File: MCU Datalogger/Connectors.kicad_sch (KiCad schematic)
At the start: 4 parts, among them J1 Conn_01x04_Pin, J2 Conn_01x04_Pin, J3 Conn_01x09_Pin, J4 Conn_02x03_Odd_Even

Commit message: main: Assigned footprints to all parts
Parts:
- J1, J2: footprint (none) -> Connector_PinHeader_2.54mm:PinHeader_1x04_P2.54mm_Vertical
- J3: footprint (none) -> Connector_PinHeader_2.54mm:PinHeader_1x09_P2.54mm_Vertical
- J4: footprint (none) -> Connector_PinHeader_2.54mm:PinHeader_2x03_P2.54mm_Vertical
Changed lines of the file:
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@@
 			)
 		)
-		(property "Footprint" ""
+		(property "Footprint" "Connector_PinHeader_2.54mm:PinHeader_1x09_P2.54mm_Vertical"
 			(at 63.5 101.6 0)
 			(effects
@@
 			)
 		)
-		(property "Footprint" ""
+		(property "Footprint" "Connector_PinHeader_2.54mm:PinHeader_2x03_P2.54mm_Vertical"
 			(at 66.04 127 0)
 			(effects
@@
 			)
 		)
-		(property "Footprint" ""
+		(property "Footprint" "Connector_PinHeader_2.54mm:PinHeader_1x04_P2.54mm_Vertical"
 			(at 60.96 46.99 0)
 			(effects
@@
 			)
 		)
-		(property "Footprint" ""
+		(property "Footprint" "Connector_PinHeader_2.54mm:PinHeader_1x04_P2.54mm_Vertical"
 			(at 63.5 69.85 0)
 			(effects

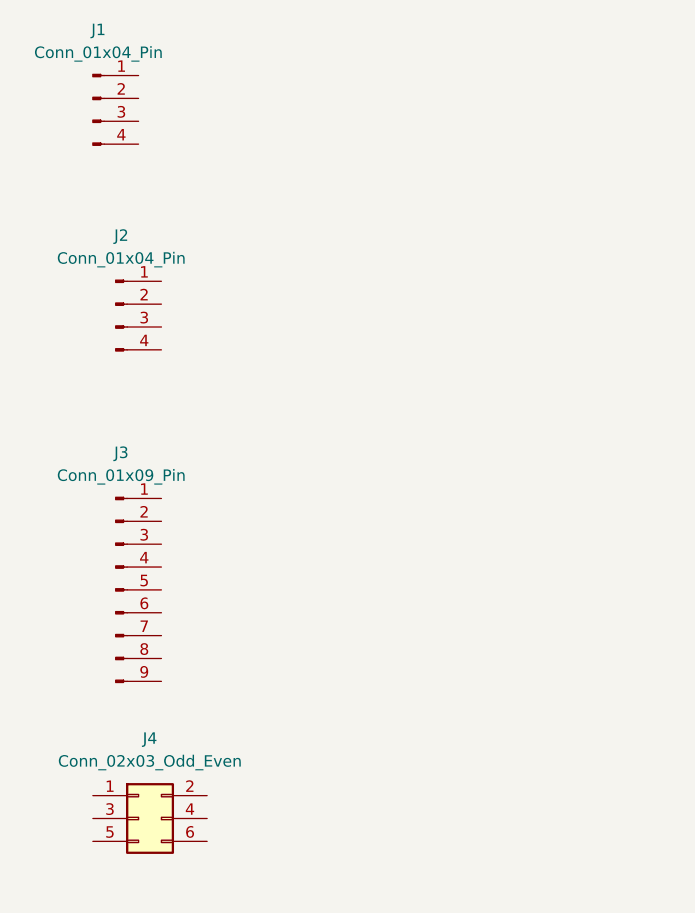
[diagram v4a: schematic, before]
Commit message: New computer update with complete schematic connections
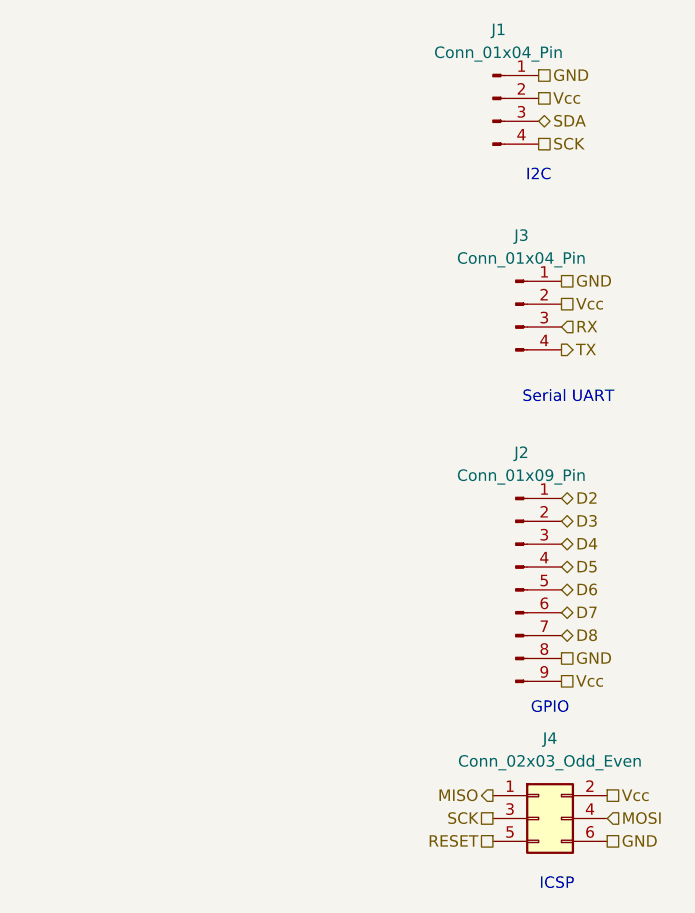
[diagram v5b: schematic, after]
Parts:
- renumbered J3 to J2, J2 to J3
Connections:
- net D2: now reaches J2.1 (Pin_1)
- net D3: now reaches J2.2 (Pin_2)
- net D4: now reaches J2.3 (Pin_3)
- net D5: now reaches J2.4 (Pin_4)
- net D6: now reaches J2.5 (Pin_5)
- net D7: now reaches J2.6 (Pin_6)
- net D8: now reaches J2.7 (Pin_7)
- net GND: now reaches J2.8 (Pin_8)
- net GND: now also J1.1 (Pin_1), J3.1 (Pin_1), J4.6 (Pin_6)
- net Vcc: now reaches J2.9 (Pin_9)
- net Vcc: now also J1.2 (Pin_2), J3.2 (Pin_2), J4.2 (Pin_2)
- net MISO: now reaches J4.1 (Pin_1)
- net SCK: now reaches J4.3 (Pin_3)
- net SCK: now also J1.4 (Pin_4)
- net MOSI: now reaches J4.4 (Pin_4)
- net RESET: now reaches J4.5 (Pin_5)
- net SDA: now reaches J1.3 (Pin_3)
- net RX: now reaches J3.3 (Pin_3)
- net TX: now reaches J3.4 (Pin_4)
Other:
- note added: "GPIO"
- note added: "I2C"
- note added: "ICSP"
- note added: "Serial UART"
- moved on the sheet: J1, J2, J3, J4

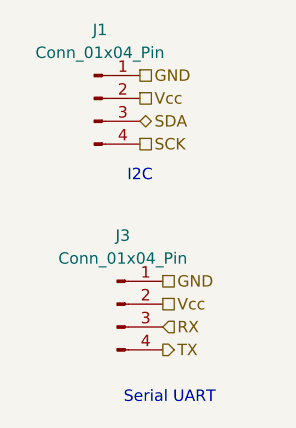
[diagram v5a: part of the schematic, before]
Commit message: main: updated schematic due to SCL and SCK mixup
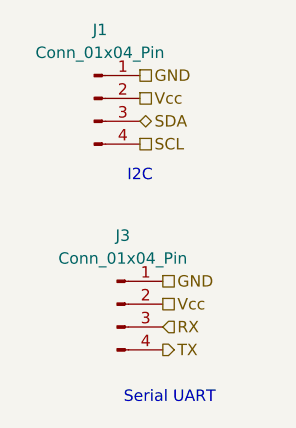
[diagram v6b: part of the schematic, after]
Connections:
- net SCK: no longer J1.4 (Pin_4)
- new net SCL: J1.4 (Pin_4)
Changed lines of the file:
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@@
 		)
 	)
-	(hierarchical_label "SCK"
+	(hierarchical_label "SCL"
 		(shape passive)
 		(at 110.49 52.07 0)
